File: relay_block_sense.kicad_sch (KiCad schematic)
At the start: 49 parts, among them J7 Screw_Terminal_01x02, J8 Screw_Terminal_01x10, J9 Screw_Terminal_01x10, U26 TLP3558A, U27 TLP3558A, U28 TLP222A, U29 TLP222A, U30 TLP222A, U31 TLP222A, U32 TLP222A, U33 TLP222A, U34 TLP222A, U35 TLP222A, U36 TLP222A, U37 TLP222A, U38 TLP222A, U39 TLP222A, U40 TLP222A, U41 TLP222A, U42 TLP222A, U43 TLP222A, U44 TLP222A, U45 TLP222A, U46 TLP222A, U47 TLP222A

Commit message: Updated documentation
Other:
- note added: "OUT B in the manual"
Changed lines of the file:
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@@
+    (effects (font (size 1.27 1.27)) (justify left bottom))
+  )
+  (text "OUT B in the manual" (at 55.88 25.4 0)
     (effects (font (size 1.27 1.27)) (justify left bottom))
   )

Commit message: Updated BOM
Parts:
- U26: Alternative Toshiba TLP3558A(F -> (none); PN TLP3558A -> TLP3558A(F
- U27: Alternative TLP3558A(F -> (none); PN TLP3558A -> TLP3558A(F
- U28, U29, U30, U31, U32, U33, U34, U35, U36, U38, U39, U40, U41, U42, U43, U44, U45, U46, U47: value TLP222A -> TLP3558A; MFN (none) -> Toshiba; PN (none) -> TLP3558A(F
- U37: value TLP222A -> TLP3558A

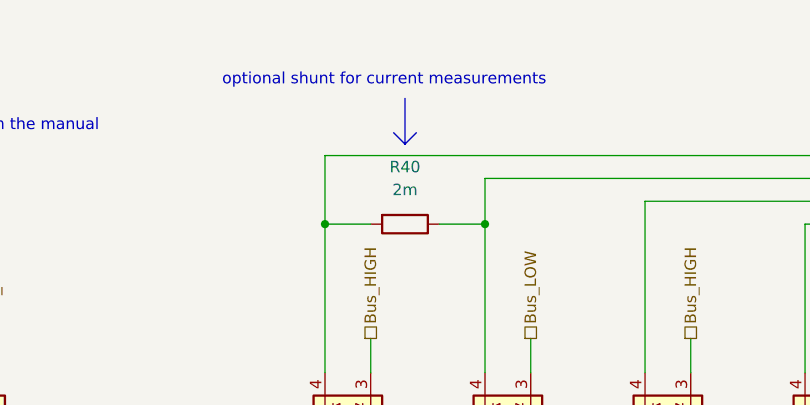
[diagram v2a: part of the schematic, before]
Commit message: Updated to KiCad 8 (#1)
- Updated libraries
- Updated BOM, replaced obsolete parts
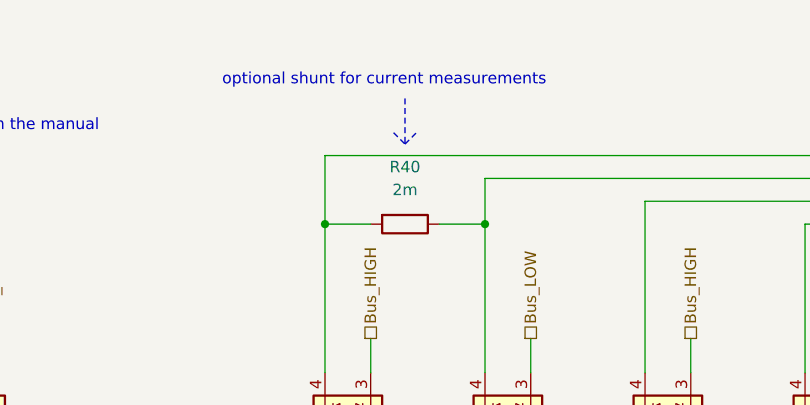
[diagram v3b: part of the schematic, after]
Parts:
- J7, J8, J9: RoHS (none) -> By exemption; Temperature (none) -> Tstorage = –40 °C to 105 °C
- R36, R37, R38, R39, R42, R43, R44, R45, R46, R47, R48, R49, R50, R51, R52, R53, R54, R55, R56, R57, R58, R59: RoHS (none) -> By exemption; Temperature (none) -> Tstorage = –55 °C to 155 °C
- R40, R41: RoHS (none) -> Yes; Temperature (none) -> Tstorage = –55 °C to 170 °C
- U26, U27, U28, U29, U30, U31, U32, U33, U34, U35, U36, U37, U38, U39, U40, U41, U42, U43, U44, U45, U46, U47: RoHS (none) -> Yes; Temperature (none) -> Tstorage = –20 °C to 85 °C
